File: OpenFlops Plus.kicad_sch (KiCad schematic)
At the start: 80 parts, among them J1 Conn_02x05_Odd_Even, J2 Conn_02x05_Odd_Even, J3 Conn_01x04, P1 Conn_02x17_Odd_Even, P2 171826-4, P3 Conn_01x04, P4 Micro_SD_Card_Det1, P5 Conn_01x04, P6 Conn_01x05, Q1 BSS138, Q2 BSS138, Q3 BSS138, Q4 BSS138, Q5 BSS138, Q6 BSS138, Q7 SS8050, SW1 BT_RIGHT, SW2 BT_LEFT, U1 AMS1117-3.3, U2 STM32F105RBT6, U3 74HCT04, U4 CH213K, U5 SRV05-4, Y1 8MHz

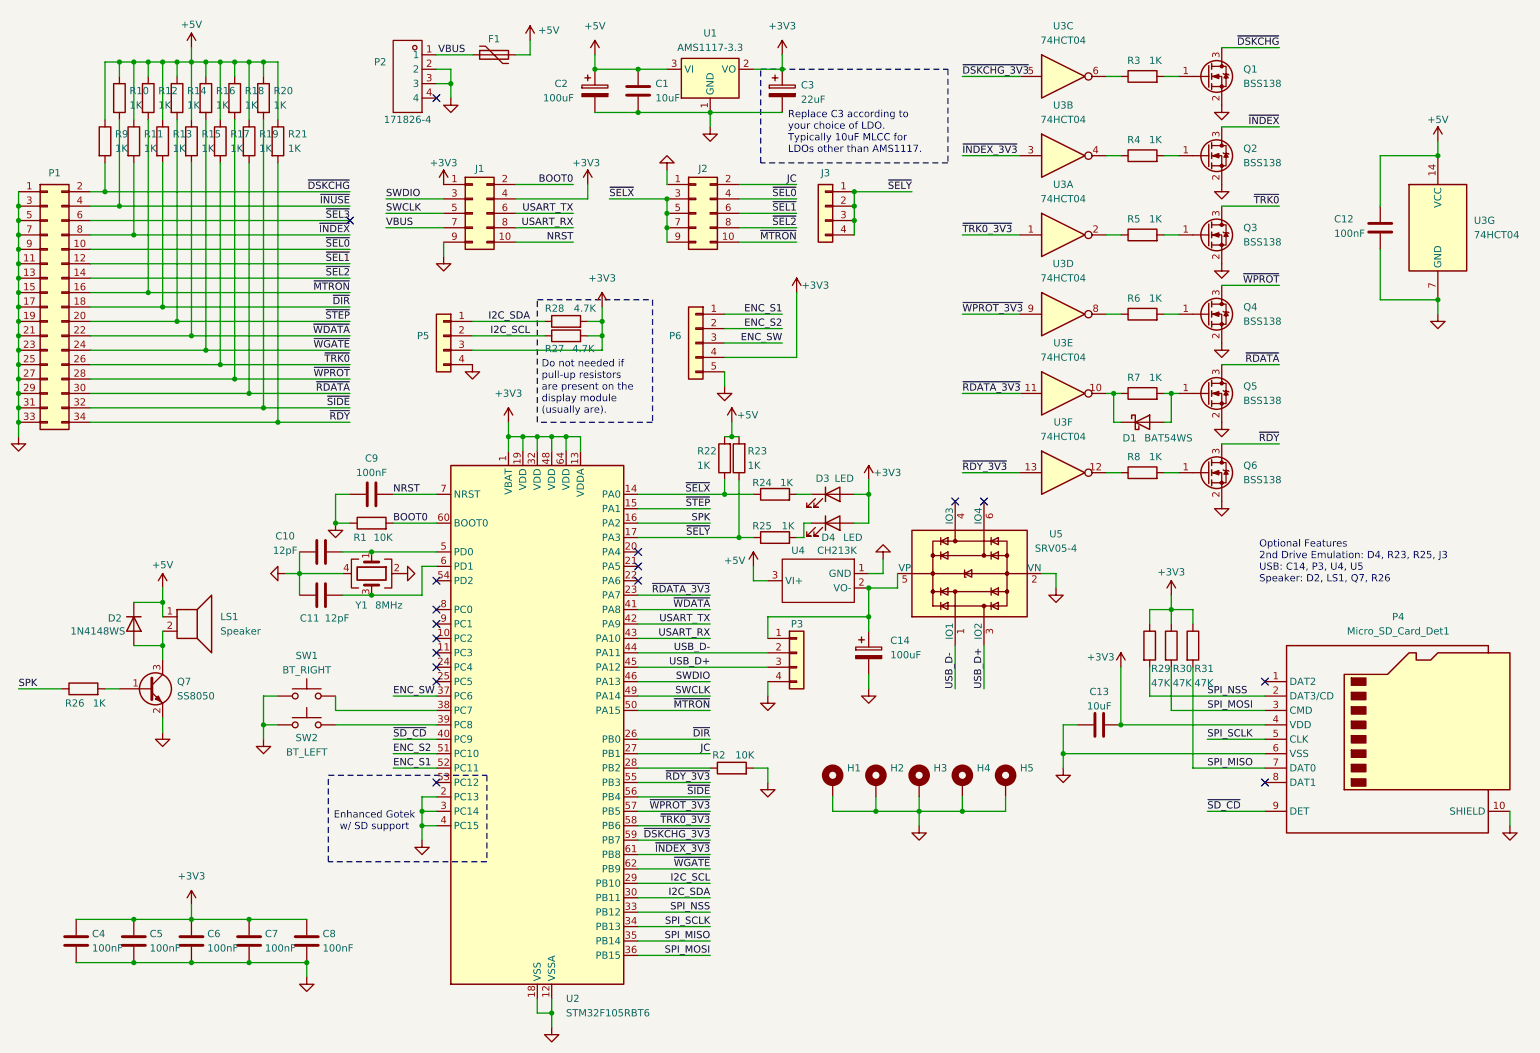
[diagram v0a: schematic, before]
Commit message: Add PMOS for card reader
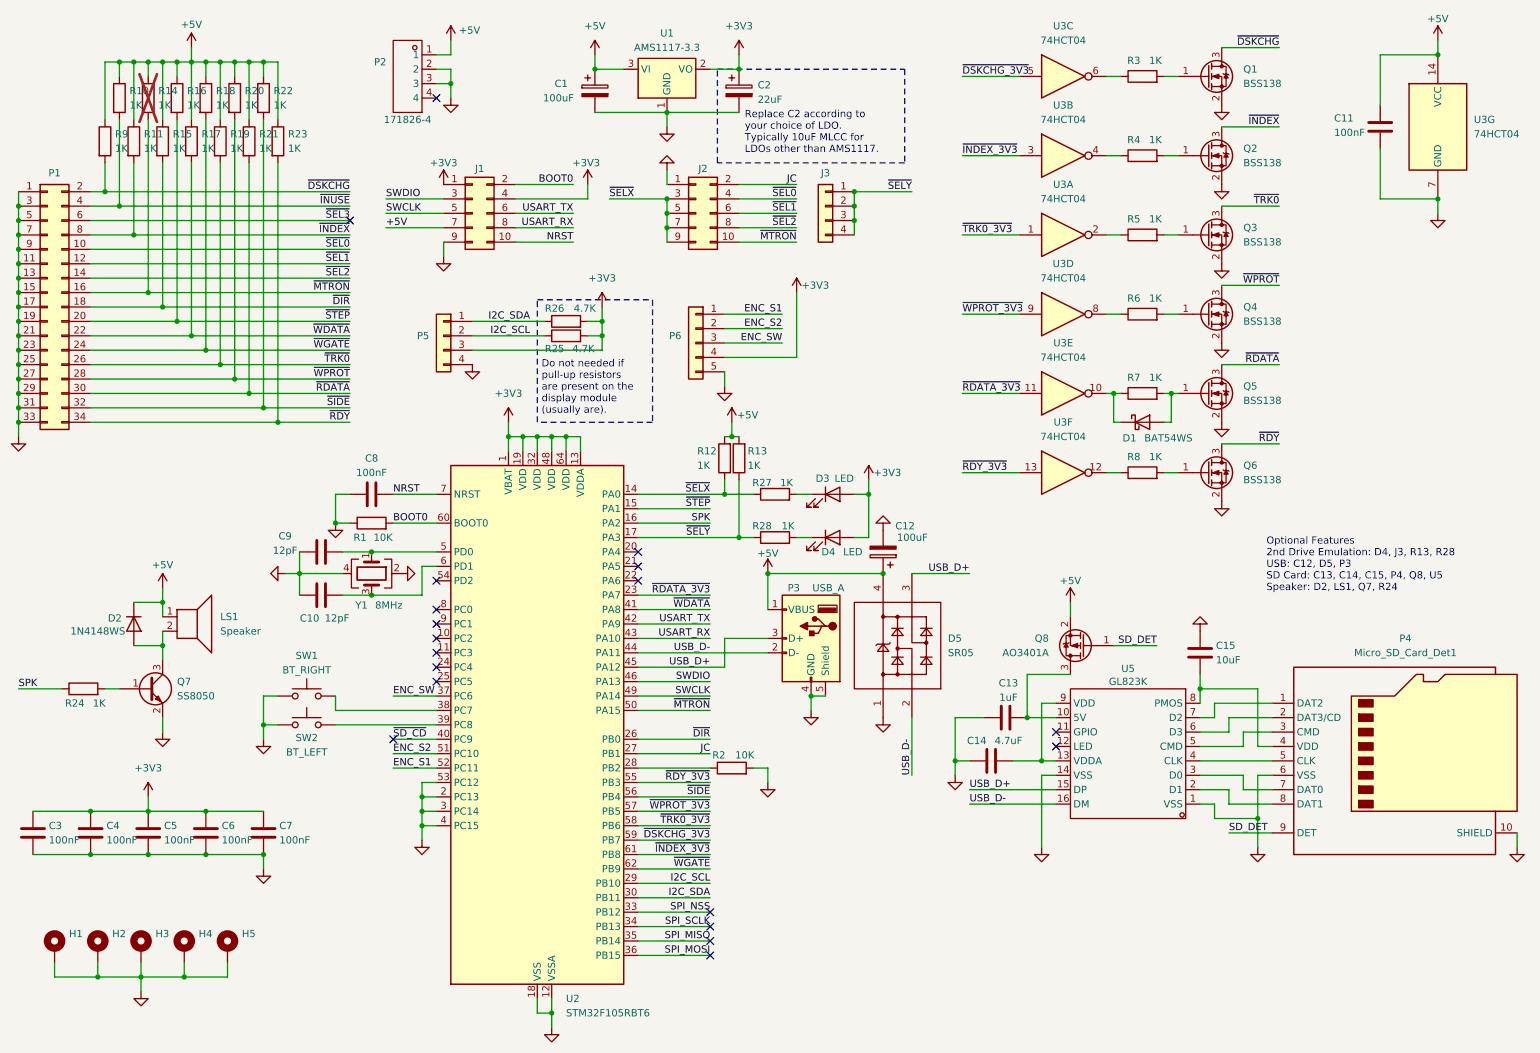
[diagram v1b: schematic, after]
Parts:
- removed C1: 10uF, Capacitor_SMD:C_1206_3216Metric, symbol Device:C
- removed F1: Polyfuse, Fuse:Fuse_1206_3216Metric, symbol Device:Polyfuse
- removed P3: Conn_01x04, Connector_PinHeader_2.54mm:PinHeader_1x04_P2.54mm_Vertical, symbol Connector_Generic:Conn_01x04
- removed R29, R30, R31: 47K, Resistor_SMD:R_0603_1608Metric, symbol Device:R
- removed U4: CH213K, Package_TO_SOT_SMD:SOT-23, symbol EasyEDA_Lib:CH213K
- removed U5: SRV05-4, Package_TO_SOT_SMD:SOT-23-6, symbol Power_Protection:SRV05-4
- added C14: 4.7uF, Capacitor_SMD:C_0603_1608Metric, symbol Device:C
- added C15: 10uF, Capacitor_SMD:C_0805_2012Metric, symbol Device:C
- added D5: SR05, Package_TO_SOT_SMD:SOT-143, symbol EasyEDA_Lib:SR05.TCT
- added P3: USB_A, Connector_USB:USB_A_Molex_67643_Horizontal, symbol Connector:USB_A
- added Q8: AO3401A, Package_TO_SOT_SMD:SOT-23, symbol Transistor_FET:AO3401A
- added U5: GL823K, Package_SO:SSOP-16_3.9x4.9mm_P0.635mm, symbol EasyEDA_Lib:GL823K-HCY04
- C13: value 10uF -> 1uF
- R14: renamed from R12; now not fitted
- renumbered C2 to C1, C11 to C10, C12 to C11, C14 to C12, C3 to C2, C4 to C3, C5 to C4, C6 to C5, C7 to C6, C8 to C7, C9 to C8, C10 to C9, R22 to R12, R23 to R13, R13 to R15, R14 to R16, R15 to R17, R16 to R18, R17 to R19, R18 to R20, R19 to R21, R20 to R22, R21 to R23, R26 to R24, R27 to R25, R28 to R26, R24 to R27, R25 to R28
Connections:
- net VBUS is gone; now on net +5V: J1.7 (Pin_7), P2.1
- net +3V3: no longer C13.2, P4.4 (VDD)
- net +5V: now also C12.1, D5.4, P3.1 (VBUS), Q8.2 (S)
- net GND: now also U2.53 (PC12), C14.1, C15.1, D5.1, P3.4 (GND), P3.5 (Shield), U5.1 (VSS), U5.14 (VSS)
- net SPI_MISO: no longer P4.7 (DAT0)
- net SPI_MOSI: no longer P4.3 (CMD)
- net SPI_NSS: no longer P4.2 (DAT3/CD)
- net SPI_SCLK: no longer P4.5 (CLK)
- net USB_D+: now also D5.3, P3.3 (D+), U5.15 (DP)
- net USB_D-: now also D5.2, P3.2 (D-), U5.16 (DM)
- net ~{SD_CD}: no longer P4.9 (DET)
- net at P4.1 (DAT2): now also U5.7 (D2)
- net at P4.8 (DAT1): now also U5.2 (D1)
- new net: C13.2, Q8.3 (D), U5.10 (5V)
- new net: C14.2, U5.13 (VDDA), U5.9 (VDD)
- new net: P4.7 (DAT0), U5.3 (D0)
- new net: P4.5 (CLK), U5.4 (CLK)
- new net: P4.3 (CMD), U5.5 (CMD)
- new net: P4.2 (DAT3/CD), U5.6 (D3)
- new net: C15.2, P4.4 (VDD), U5.8 (PMOS)
- new net SD_DET: P4.9 (DET), Q8.1 (G)
- no-connect marks 17 -> 19
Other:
- note added: "Optional Features 2nd Drive Emulation: D4, J3, R13, R28 USB: C12, D5, P3 SD Card: C13, C14, C15, P4, Q8, U5 Speaker: D2, LS1, Q7, R24"
- note added: "Replace C2 according to your choice of LDO. Typically 10uF MLCC for LDOs other than AMS1117."
- note removed: "Enhanced Gotek w/ SD support"
- note removed: "Optional Features 2nd Drive Emulation: D4, R23, R25, J3 USB: C14, P3, U4, U5 Speaker: D2, LS1, Q7, R26"
- note removed: "Replace C3 according to your choice of LDO. Typically 10uF MLCC for LDOs other than AMS1117."
- moved on the sheet: C11, C12, C2, C3, C4, C5, C6, C7, D4, H1, H2, H3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

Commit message: Move to 74LS07
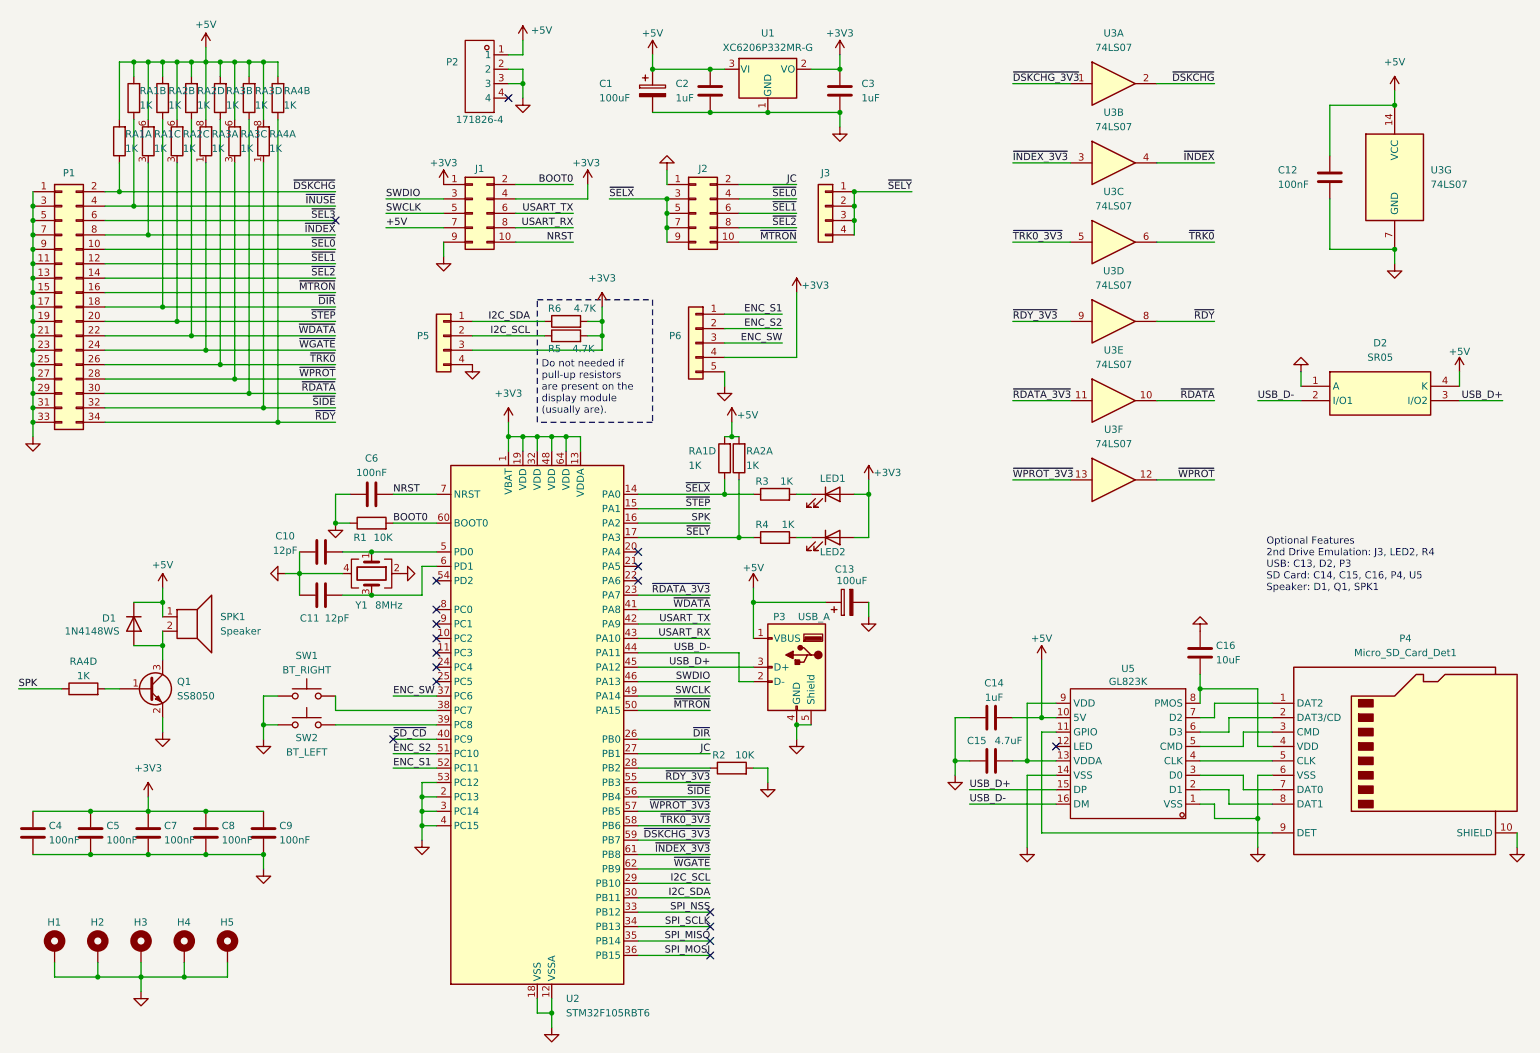
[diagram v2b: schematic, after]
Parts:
- removed C11: 100nF, Capacitor_SMD:C_0603_1608Metric, symbol Device:C
- removed C2: 22uF, Capacitor_SMD:C_1206_3216Metric, symbol Device:C_Polarized
- removed D1: BAT54WS, Diode_SMD:D_SOD-323, symbol Diode:BAT54J
- removed D5: SR05, Package_TO_SOT_SMD:SOT-143, symbol EasyEDA_Lib:SR05.TCT
- removed Q1, Q2, Q3, Q4, Q5, Q6: BSS138, Package_TO_SOT_SMD:SOT-23, symbol Transistor_FET:BSS138
- removed Q8: AO3401A, Package_TO_SOT_SMD:SOT-23, symbol Transistor_FET:AO3401A
- removed R10, R11, R12, R13, R14, R15, R16, R17, R18, R19, R20, R21, R22, R23, R24, R3, R4, R5, R6, R7, R8, R9: 1K, Resistor_SMD:R_0603_1608Metric, symbol Device:R
- removed U1: AMS1117-3.3, Package_TO_SOT_SMD:SOT-223-3_TabPin2, symbol Regulator_Linear:AMS1117-3.3
- removed U3: 74HCT04, Package_SO:SOIC-14_3.9x8.7mm_P1.27mm, symbol 74xx:74HC04
- added C12: 100nF, Capacitor_SMD:C_0603_1608Metric, symbol Device:C
- added C2, C3: 1uF, Capacitor_SMD:C_0603_1608Metric, symbol Device:C
- added D2: SR05, Package_TO_SOT_SMD:SOT-143, symbol SR05_TCT:SR05.TCT
- added RA1, RA2, RA3, RA4: 1K, Resistor_SMD:R_Array_Convex_4x0603, symbol Device:R_Pack04_Split
- added U1: XC6206P332MR-G, Package_TO_SOT_SMD:SOT-23-3, symbol Regulator_Linear:XC6206PxxxMR
- added U3: 74LS07, Package_SO:SOIC-14_3.9x8.7mm_P1.27mm, symbol 74xx:74LS07
- renumbered C9 to C10, C10 to C11, C12 to C13, C13 to C14, C14 to C15, C15 to C16, C3 to C4, C4 to C5, C8 to C6, C5 to C7, C6 to C8, C7 to C9, D2 to D1, D3 to LED1, D4 to LED2, Q7 to Q1, R27 to R3, R28 to R4, R25 to R5, R26 to R6, LS1 to SPK1
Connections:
- net SD_DET is gone; now on an unnamed net: P4.9 (DET)
- net +3V3: now also C3.1, U1.2 (VO)
- net +5V: now also C14.2, U5.10 (5V), C12.1, C2.1, D2.4 (K), RA1.5 (R4.2), RA1.6 (R3.2), RA1.7 (R2.2), RA1.8 (R1.2), RA2.5 (R4.2), RA2.6 (R3.2), RA2.7 (R2.2), RA2.8 (R1.2), RA3.5 (R4.2), RA3.6 (R3.2), RA3.7 (R2.2), RA3.8 (R1.2), RA4.7 (R2.2), RA4.8 (R1.2), U1.3 (VI), U3.14 (VCC)
- net GND: now also C12.2, C2.2, C3.2, D2.1 (A), U1.1 (GND), U3.7 (GND)
- net SPK: now also RA4.4 (R4.1)
- net USB_D+: now also D2.3 (I/O2)
- net USB_D-: now also D2.2 (I/O1)
- net ~{DIR}: now also RA2.2 (R2.1)
- net ~{DSKCHG_3V3}: now also U3.1
- net ~{DSKCHG}: now also RA1.1 (R1.1), U3.2
- net ~{INDEX_3V3}: now also U3.3
- net ~{INDEX}: now also RA1.3 (R3.1), U3.4
- net ~{INUSE}: now also RA1.2 (R2.1)
- net ~{RDATA_3V3}: now also U3.11
- net ~{RDATA}: now also RA3.4 (R4.1), U3.10
- net ~{RDY_3V3}: now also U3.9
- net ~{RDY}: now also RA4.2 (R2.1), U3.8
- net ~{SELX}: now also RA1.4 (R4.1)
- net ~{SELY}: now also RA2.1 (R1.1)
- net ~{SIDE}: now also RA4.1 (R1.1)
- net ~{STEP}: now also RA2.3 (R3.1)
- net ~{TRK0_3V3}: now also U3.5
- net ~{TRK0}: now also RA3.2 (R2.1), U3.6
- net ~{WDATA}: now also RA2.4 (R4.1)
- net ~{WGATE}: now also RA3.1 (R1.1)
- net ~{WPROT_3V3}: now also U3.13
- net ~{WPROT}: now also RA3.3 (R3.1), U3.12
- net at Q1.1 (B): now also RA4.5 (R4.2)
- no-connect marks 19 -> 18
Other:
- note added: "Optional Features 2nd Drive Emulation: J3, LED2, R4 USB: C13, D2, P3 SD Card: C14, C15, C16, P4, U5 Speaker: D1, Q1, SPK1"
- note removed: "Optional Features 2nd Drive Emulation: D4, J3, R13, R28 USB: C12, D5, P3 SD Card: C13, C14, C15, P4, Q8, U5 Speaker: D2, LS1, Q7, R24"
- note removed: "Replace C2 according to your choice of LDO. Typically 10uF MLCC for LDOs other than AMS1117."
- moved on the sheet: C13, C14, P1, P2, P3

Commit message: Use SPI to manipulate SD card
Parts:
- removed C15: 4.7uF, Capacitor_SMD:C_0603_1608Metric, symbol Device:C
- removed C16: 10uF, Capacitor_SMD:C_0805_2012Metric, symbol Device:C
- removed U5: GL823K, Package_SO:SSOP-16_3.9x4.9mm_P0.635mm, symbol EasyEDA_Lib:GL823K-HCY04
- added C13: 10uF, Capacitor_SMD:C_0805_2012Metric, symbol Device:C
- added J4: Conn_01x04, Connector_PinHeader_2.54mm:PinHeader_1x04_P2.54mm_Vertical, symbol Connector_Generic:Conn_01x04
- added Q2: BSS138, Package_TO_SOT_SMD:SOT-23, symbol Transistor_FET:BSS138
- added R7: 47K, Resistor_SMD:R_0603_1608Metric, symbol Device:R
- added R8: 10K, Resistor_SMD:R_0603_1608Metric, symbol Device:R
- added unit 3 of RA4
- C14: value 1uF -> 100nF
- U1: value XC6206P332MR-G -> ME6211A33M3G-N
- renumbered C13 to C15, R5 to R3, R6 to R4, R3 to R5, R4 to R6
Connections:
- net +3V3: now also C14.1, P4.4 (VDD), R5.2, R6.2, C13.1, R7.1, R8.1; no longer LED1.2 (A), LED2.2 (A)
- net +5V: now also J4.1 (Pin_1), RA4.6 (R3.2); no longer C14.2
- net GND: now also C14.2, C13.2, J4.4 (Pin_4), Q2.2 (S); no longer C14.1, U2.53 (PC12)
- net SPI_MISO: now also P4.7 (DAT0)
- net SPI_MOSI: now also P4.3 (CMD)
- net SPI_NSS: now also P4.2 (DAT3/CD), R7.2
- net SPI_SCLK: now also P4.5 (CLK)
- net SPK: now also RA4.5 (R4.2); no longer RA4.4 (R4.1)
- net USB_D+: now also J4.3 (Pin_3)
- net USB_D-: now also J4.2 (Pin_2)
- net ~{DIR}: now also RA2.3 (R3.1); no longer RA2.2 (R2.1)
- net ~{MTRON}: now also RA2.2 (R2.1)
- net ~{RDATA}: now also RA4.1 (R1.1); no longer RA3.4 (R4.1)
- net ~{RDY}: now also RA4.3 (R3.1); no longer RA4.2 (R2.1)
- net ~{SD_CD}: now also P4.9 (DET), Q2.1 (G), R8.2; no longer U2.40 (PC9)
- net ~{SELX}: now also LED1.1 (K); no longer R5.1
- net ~{SELY}: now also LED2.1 (K); no longer R6.1
- net ~{SIDE}: now also RA4.2 (R2.1); no longer RA4.1 (R1.1)
- net ~{STEP}: now also RA2.4 (R4.1); no longer RA2.3 (R3.1)
- net ~{TRK0}: now also RA3.3 (R3.1); no longer RA3.2 (R2.1)
- net ~{WDATA}: now also RA3.1 (R1.1); no longer RA2.4 (R4.1)
- net ~{WGATE}: now also RA3.2 (R2.1); no longer RA3.1 (R1.1)
- net ~{WPROT}: now also RA3.4 (R4.1); no longer RA3.3 (R3.1)
- net at Q1.1 (B): now also RA4.4 (R4.1); no longer RA4.5 (R4.2)
- new net: LED1.2 (A), R5.1
- new net: LED2.2 (A), R6.1
- new net SD_CD: Q2.3 (D), U2.40 (PC9)
- no-connect marks 18 -> 15
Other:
- note added: "Optional Features 2nd Drive Emulation: J3, LED2, R6 USB: C15, D2, P3 / J4 SD Card: C13, C14, P4, Q2, R7, R8 Speaker: D1, Q1, SPK1"
- note removed: "Optional Features 2nd Drive Emulation: J3, LED2, R4 USB: C13, D2, P3 SD Card: C14, C15, C16, P4, U5 Speaker: D1, Q1, SPK1"
- moved on the sheet: D2, LED1, LED2, P4, R5, R6
